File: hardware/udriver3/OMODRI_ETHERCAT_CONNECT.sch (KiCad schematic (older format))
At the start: 2 parts, among them J15 ADM6_ADF6, J16 ADM6_ADF6

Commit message: Update of the PCB routing. - F.paste updated on BGA (removed) and Q1 to Q6 (as proposed in datasheet) - F.SilkS and B.SilkS updated
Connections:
- net GND: no longer J15.C02, J15.C04, J15.C06, J15.C08, J15.D02, J15.D04, J15.D06, J15.D08, J16.A03, J16.A05, J16.A07, J16.A09, J16.B03, J16.B05, J16.B07, J16.B08, J16.B09
- new net VDD_3V3: J15.C02, J15.C04, J15.C06, J15.C08, J15.D02, J15.D04, J15.D06, J15.D08, J16.A03, J16.A05, J16.A07, J16.A09, J16.B03, J16.B05, J16.B07, J16.B08, J16.B09
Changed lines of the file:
@@
-$Comp
-L omodri_lib:ADM6_ADF6 J?
-U 1 1 5FA3E1D7
-P 3400 3250
-AR Path="/5FA3E1D7" Ref="J?"  Part="1"
-AR Path="/5F5975A7/5FA2AE4C/5FA3E1D7" Ref="J16"  Part="1"
-F 0 "J16" H 3400 3800 50  0000 L CNN
-F 1 "ADM6_ADF6" H 3400 2700 50  0000 L CNN
-F 2 "udriver3:ADF6-10-XX.X-XXX-4-X-A-XR" H 3400 3250 50  0001 C CNN
-F 3 "http://suddendocs.samtec.com/prints/adf6-xxx-xx.x-xxx-4-x-x-xr-mkt.pdf" H 3400 3250 50  0001 C CNN
-F 4 "612-ADF6-10-03.5-L-4-2-A-TR-ND" H 3400 3250 50  0001 C CNN "DigiKey"
-F 5 "3462763" H 3400 3250 50  0001 C CNN "Farnell"
-F 6 "200-ADF6-10-3.5-L42A" H 3400 3250 50  0001 C CNN "Mouser"
-F 7 "ADF6-10-03.5-L-4-2-A" H 3400 3250 50  0001 C CNN "Part No"
-F 8 "202-7885" H 3400 3250 50  0001 C CNN "RS"
-	1    3400 3250
-	1    0    0    -1
-$EndComp
 $Comp
 L omodri_lib:ADM6_ADF6 J?
@@
 Text HLabel 7350 3000 0    50   Output ~ 0
 ESC_RX1_DV
-Text HLabel 3025 2800 0    50   Output ~ 0
-ESC_RX1_ERR
 Text HLabel 4325 2900 0    50   Output ~ 0
 ESC_RX1_CLK
@@
 Text HLabel 7350 3200 0    50   Input ~ 0
 ESC_TX1_ENA
-Text HLabel 3025 3100 0    50   Output ~ 0
-ESC_TX1_CLK
 Text HLabel 7325 4700 0    50   Output ~ 0
 ESC_TX0_CLK
 Text HLabel 3025 4600 0    50   Input ~ 0
 ~ESC_PHY_RESETn~
-Text HLabel 3025 3500 0    50   Input ~ 0
-ESC_PHY_CLK_OSC
 Text HLabel 5850 3000 0    50   Input ~ 0
 ESC_PHY_CLK_INT
@@
 Text HLabel 5850 4500 0    50   Output ~ 0
 ESC_PHY0_LINKSTATUS
-Text HLabel 3025 2900 0    50   Output ~ 0
-ESC_PHY1_LINKSTATUS
 Text HLabel 3025 4800 0    50   Output ~ 0
 ECAT0_INT
-Text HLabel 3025 3300 0    50   Output ~ 0
-ECAT1_INT
 $Comp
 L omodri_lib:ADM6_ADF6 J?
@@
 Wire Wire Line
 	4400 4500 4400 4700
-$Comp
-L power:GND #PWR?
-U 1 1 5FAA5B09
-P 5925 5250
-AR Path="/5F3A3F16/5FAA5B09" Ref="#PWR?"  Part="1"
-AR Path="/5F7A5BAE/5FAA5B09" Ref="#PWR?"  Part="1"
-AR Path="/5F497A69/5FAA5B09" Ref="#PWR?"  Part="1"
-AR Path="/5F5B5760/5FAA5B09" Ref="#PWR?"  Part="1"
-AR Path="/5F5975A7/5FA2AE4C/5FAA5B09" Ref="#PWR0162"  Part="1"
-F 0 "#PWR0162" H 5925 5000 50  0001 C CNN
-F 1 "GND" H 5930 5077 50  0000 C CNN
-F 2 "" H 5925 5250 50  0001 C CNN
-F 3 "" H 5925 5250 50  0001 C CNN
-	1    5925 5250
-	1    0    0    -1
-$EndComp
-$Comp
-L power:GND #PWR?
-U 1 1 5FAAA259
-P 7425 5250
-AR Path="/5F3A3F16/5FAAA259" Ref="#PWR?"  Part="1"
-AR Path="/5F7A5BAE/5FAAA259" Ref="#PWR?"  Part="1"
-AR Path="/5F497A69/5FAAA259" Ref="#PWR?"  Part="1"
-AR Path="/5F5B5760/5FAAA259" Ref="#PWR?"  Part="1"
-AR Path="/5F5975A7/5FA2AE4C/5FAAA259" Ref="#PWR0163"  Part="1"
-F 0 "#PWR0163" H 7425 5000 50  0001 C CNN
-F 1 "GND" H 7430 5077 50  0000 C CNN
-F 2 "" H 7425 5250 50  0001 C CNN
-F 3 "" H 7425 5250 50  0001 C CNN
-	1    7425 5250
-	1    0    0    -1
-$EndComp
 Wire Wire Line
 	3200 4500 3100 4500
@@
 Wire Wire Line
 	7350 5100 7525 5100
-$Comp
-L power:GND #PWR?
-U 1 1 5F9E52B0
-P 3100 3750
-AR Path="/5F3A3F16/5F9E52B0" Ref="#PWR?"  Part="1"
-AR Path="/5F7A5BAE/5F9E52B0" Ref="#PWR?"  Part="1"
-AR Path="/5F497A69/5F9E52B0" Ref="#PWR?"  Part="1"
-AR Path="/5F5B5760/5F9E52B0" Ref="#PWR?"  Part="1"
-AR Path="/5F5975A7/5FA2AE4C/5F9E52B0" Ref="#PWR0150"  Part="1"
-F 0 "#PWR0150" H 3100 3500 50  0001 C CNN
-F 1 "GND" H 3105 3577 50  0000 C CNN
-F 2 "" H 3100 3750 50  0001 C CNN
-F 3 "" H 3100 3750 50  0001 C CNN
-	1    3100 3750
-	1    0    0    -1
-$EndComp
 Wire Wire Line
 	3100 3750 3100 3600
 Wire Wire Line
 	3100 3600 3200 3600
-$Comp
-L power:GND #PWR?
-U 1 1 5FA1341F
-P 4400 3750
-AR Path="/5F3A3F16/5FA1341F" Ref="#PWR?"  Part="1"
-AR Path="/5F7A5BAE/5FA1341F" Ref="#PWR?"  Part="1"
-AR Path="/5F497A69/5FA1341F" Ref="#PWR?"  Part="1"
-AR Path="/5F5B5760/5FA1341F" Ref="#PWR?"  Part="1"
-AR Path="/5F5975A7/5FA2AE4C/5FA1341F" Ref="#PWR0154"  Part="1"
-F 0 "#PWR0154" H 4400 3500 50  0001 C CNN
-F 1 "GND" H 4405 3577 50  0000 C CNN
-F 2 "" H 4400 3750 50  0001 C CNN
-F 3 "" H 4400 3750 50  0001 C CNN
-	1    4400 3750
-	1    0    0    -1
-$EndComp
 $Comp
 L power:GND #PWR?
@@
 Wire Wire Line
 	4400 3750 4400 3600
-Wire Wire Line
-	3025 3500 3200 3500
 Wire Wire Line
 	7350 4300 7525 4300
@@
 	6025 3500 5925 3500
 Wire Wire Line
-	3025 2800 3200 2800
-Wire Wire Line
 	4325 2800 4500 2800
 Wire Wire Line
@@
 Wire Wire Line
 	4325 2900 4500 2900
-Wire Wire Line
-	3200 2900 3025 2900
 Wire Wire Line
 	7425 3500 7425 3300
@@
 Wire Wire Line
 	3100 3600 3100 3400
-Wire Wire Line
-	3100 3000 3200 3000
 Connection ~ 3100 3600
 Wire Wire Line
@@
 Wire Wire Line
 	4500 3100 4325 3100
-Wire Wire Line
-	3200 3100 3025 3100
-Text HLabel 3025 3700 0    50   Output ~ 0
-COM_SPI_SIMO
 Text HLabel 5850 3600 0    50   Input ~ 0
 COM_SPI_SOMI
@@
 	6025 3700 5925 3700
 Wire Wire Line
-	3200 3700 3025 3700
-Wire Wire Line
 	4500 3700 4325 3700
 Wire Wire Line
 	3100 3200 3200 3200
-Connection ~ 3100 3200
-Wire Wire Line
-	3100 3200 3100 3000
 Wire Wire Line
 	4500 3200 4400 3200
@@
 	6025 3200 5850 3200
 Wire Wire Line
-	3200 3300 3025 3300
-Wire Wire Line
 	7525 3300 7425 3300
 Connection ~ 7425 3300
@@
 Wire Wire Line
 	5925 3700 5925 3750
+$Comp
+L omodri_lib:ADM6_ADF6 J?
+U 1 1 5FA3E1D7
+P 3400 3250
+AR Path="/5FA3E1D7" Ref="J?"  Part="1"
+AR Path="/5F5975A7/5FA2AE4C/5FA3E1D7" Ref="J16"  Part="1"
+F 0 "J16" H 3400 3800 50  0000 L CNN
+F 1 "ADM6_ADF6" H 3400 2700 50  0000 L CNN
+F 2 "udriver3:ADF6-10-XX.X-XXX-4-X-A-XR" H 3400 3250 50  0001 C CNN
+F 3 "http://suddendocs.samtec.com/prints/adf6-xxx-xx.x-xxx-4-x-x-xr-mkt.pdf" H 3400 3250 50  0001 C CNN
+F 4 "612-ADF6-10-03.5-L-4-2-A-TR-ND" H 3400 3250 50  0001 C CNN "DigiKey"
+F 5 "3462763" H 3400 3250 50  0001 C CNN "Farnell"
+F 6 "200-ADF6-10-3.5-L42A" H 3400 3250 50  0001 C CNN "Mouser"
+F 7 "ADF6-10-03.5-L-4-2-A" H 3400 3250 50  0001 C CNN "Part No"
+F 8 "202-7885" H 3400 3250 50  0001 C CNN "RS"
+	1    3400 3250
+	1    0    0    -1
+$EndComp
+Connection ~ 3100 3200
+Wire Wire Line
+	3100 3200 3100 3000
+Wire Wire Line
+	3100 3000 3200 3000
+Text GLabel 3100 3750 3    50   Input ~ 0
+VDD_3V3
+Wire Wire Line
+	3200 3300 3025 3300
+Wire Wire Line
+	3200 3700 3025 3700
+Text HLabel 3025 3700 0    50   Output ~ 0
+COM_SPI_SIMO
+Wire Wire Line
+	3200 3100 3025 3100
+Wire Wire Line
+	3200 2900 3025 2900
+Wire Wire Line
+	3025 2800 3200 2800
+Wire Wire Line
+	3025 3500 3200 3500
+Text HLabel 3025 3300 0    50   Output ~ 0
+ECAT1_INT
+Text HLabel 3025 2900 0    50   Output ~ 0
+ESC_PHY1_LINKSTATUS
+Text HLabel 3025 3500 0    50   Input ~ 0
+ESC_PHY_CLK_OSC
+Text HLabel 3025 3100 0    50   Output ~ 0
+ESC_TX1_CLK
+Text HLabel 3025 2800 0    50   Output ~ 0
+ESC_RX1_ERR
+Text GLabel 4400 3750 3    50   Input ~ 0
+VDD_3V3
+Text GLabel 5925 5250 3    50   Input ~ 0
+VDD_3V3
+Text GLabel 7425 5250 3    50   Input ~ 0
+VDD_3V3
 $EndSCHEMATC

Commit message: Revision of the OMODRI PCB including: - 5V power distribution on extension connector - New GPIO pin available on extension connector for SPI chip select (SSI sensors) - Connectors labels - logos - BGA solder mask/past updated
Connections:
- net GND: no longer J16.C10, J16.D10
- net VDD_3V3: no longer J16.B08
- new net 5V0: J16.C10, J16.D10
- new net ~SPI_CS2n~: J16.B08
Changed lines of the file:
@@
-$Comp
-L omodri_lib:ADM6_ADF6 J?
-U 2 1 5FA3E1DD
-P 4700 3250
-AR Path="/5FA3E1DD" Ref="J?"  Part="2"
-AR Path="/5F5975A7/5FA2AE4C/5FA3E1DD" Ref="J16"  Part="2"
-F 0 "J16" H 4700 3800 50  0000 L CNN
-F 1 "ADM6_ADF6" H 4700 2700 50  0000 L CNN
-F 2 "udriver3:ADF6-10-XX.X-XXX-4-X-A-XR" H 4700 3250 50  0001 C CNN
-F 3 "http://suddendocs.samtec.com/prints/adf6-xxx-xx.x-xxx-4-x-x-xr-mkt.pdf" H 4700 3250 50  0001 C CNN
-F 4 "612-ADF6-10-03.5-L-4-2-A-TR-ND" H 4700 3250 50  0001 C CNN "DigiKey"
-F 5 "3462763" H 4700 3250 50  0001 C CNN "Farnell"
-F 6 "200-ADF6-10-3.5-L42A" H 4700 3250 50  0001 C CNN "Mouser"
-F 7 "ADF6-10-03.5-L-4-2-A" H 4700 3250 50  0001 C CNN "Part No"
-F 8 "202-7885" H 4700 3250 50  0001 C CNN "RS"
-	2    4700 3250
-	1    0    0    -1
-$EndComp
 $Comp
 L omodri_lib:ADM6_ADF6 J?
@@
 Connection ~ 3100 3600
 Wire Wire Line
-	4400 3600 4400 3500
-Wire Wire Line
 	4400 3000 4500 3000
 Connection ~ 4400 3600
@@
 COM_SPI_CLK
 Wire Wire Line
-	7425 3500 7425 3700
-Wire Wire Line
-	6025 3700 5925 3700
-Wire Wire Line
 	4500 3700 4325 3700
 Wire Wire Line
@@
 	6025 3400 5850 3400
 Wire Wire Line
-	4500 3500 4400 3500
-Connection ~ 4400 3500
-Wire Wire Line
-	4400 3500 4400 3400
-Wire Wire Line
-	5925 3500 5925 3700
-Wire Wire Line
 	6025 3600 5850 3600
-Connection ~ 7425 3700
-Wire Wire Line
-	7425 3700 7425 3750
-Wire Wire Line
-	7425 3700 7525 3700
-Connection ~ 5925 3700
-Wire Wire Line
-	5925 3700 5925 3750
 $Comp
 L omodri_lib:ADM6_ADF6 J?
@@
 Text GLabel 7425 5250 3    50   Input ~ 0
 VDD_3V3
+Text HLabel 4325 3500 0    50   Output ~ 0
+~SPI_CS2n~
+Wire Wire Line
+	4400 3400 4400 3600
+$Comp
+L omodri_lib:ADM6_ADF6 J?
+U 2 1 5FA3E1DD
+P 4700 3250
+AR Path="/5FA3E1DD" Ref="J?"  Part="2"
+AR Path="/5F5975A7/5FA2AE4C/5FA3E1DD" Ref="J16"  Part="2"
+F 0 "J16" H 4700 3800 50  0000 L CNN
+F 1 "ADM6_ADF6" H 4700 2700 50  0000 L CNN
+F 2 "udriver3:ADF6-10-XX.X-XXX-4-X-A-XR" H 4700 3250 50  0001 C CNN
+F 3 "http://suddendocs.samtec.com/prints/adf6-xxx-xx.x-xxx-4-x-x-xr-mkt.pdf" H 4700 3250 50  0001 C CNN
+F 4 "612-ADF6-10-03.5-L-4-2-A-TR-ND" H 4700 3250 50  0001 C CNN "DigiKey"
+F 5 "3462763" H 4700 3250 50  0001 C CNN "Farnell"
+F 6 "200-ADF6-10-3.5-L42A" H 4700 3250 50  0001 C CNN "Mouser"
+F 7 "ADF6-10-03.5-L-4-2-A" H 4700 3250 50  0001 C CNN "Part No"
+F 8 "202-7885" H 4700 3250 50  0001 C CNN "RS"
+	2    4700 3250
+	1    0    0    -1
+$EndComp
+Wire Wire Line
+	4500 3500 4325 3500
+Wire Wire Line
+	7425 3500 7425 3750
+Text GLabel 7350 3700 0    50   Input ~ 0
+5V0
+Text GLabel 5850 3700 0    50   Input ~ 0
+5V0
+Wire Wire Line
+	5925 3500 5925 3750
+Wire Wire Line
+	5850 3700 6025 3700
+Wire Wire Line
+	7350 3700 7525 3700
 $EndSCHEMATC

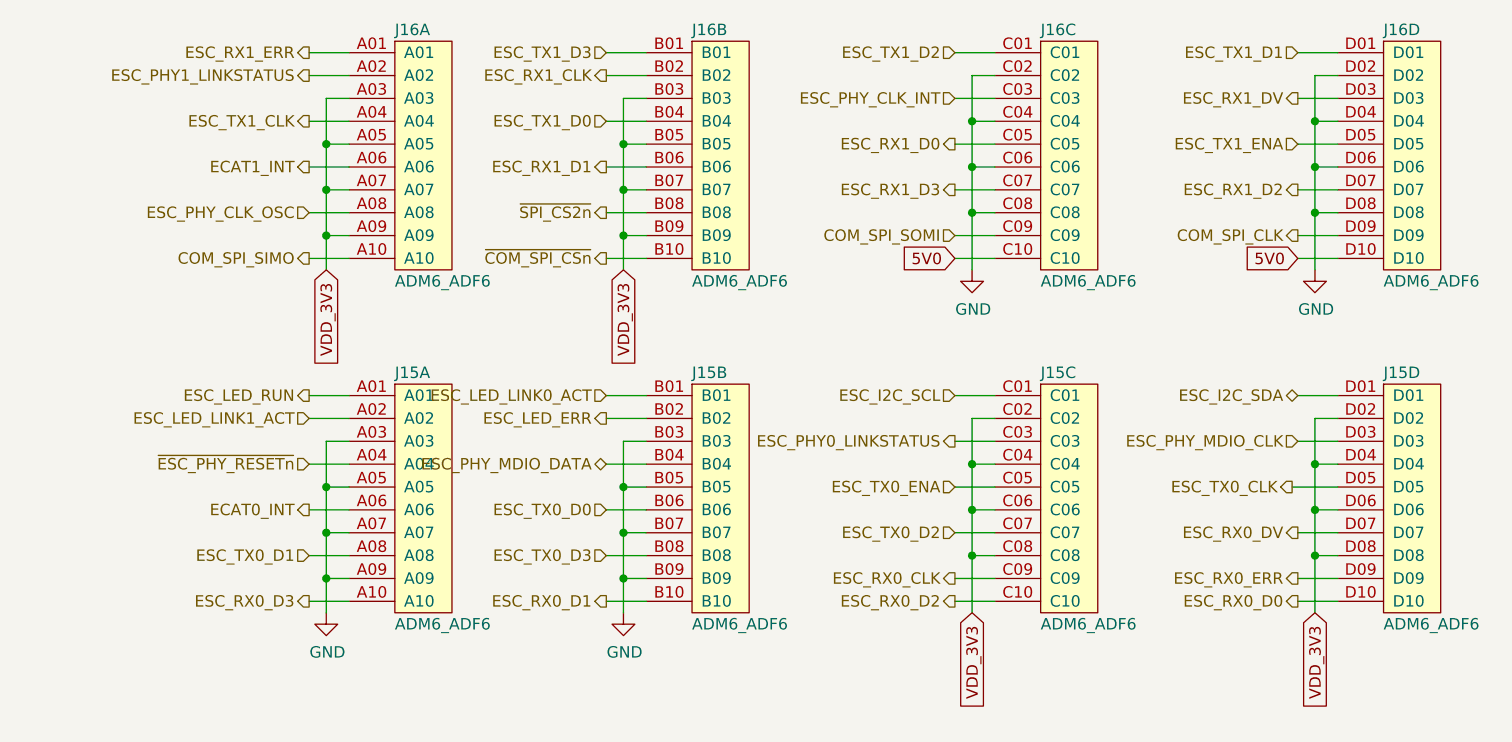
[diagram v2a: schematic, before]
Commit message: Update of µOmodri: - 25MHz oscillator signal removed (ECAT_PHY_CLK is still present) - 1x Analog signal available on extension connector - SPI on extension connector replaced. Previously SPI3/COM SPI, also available on J2, replaced by general purpose SPI2 also available on J1 connector.
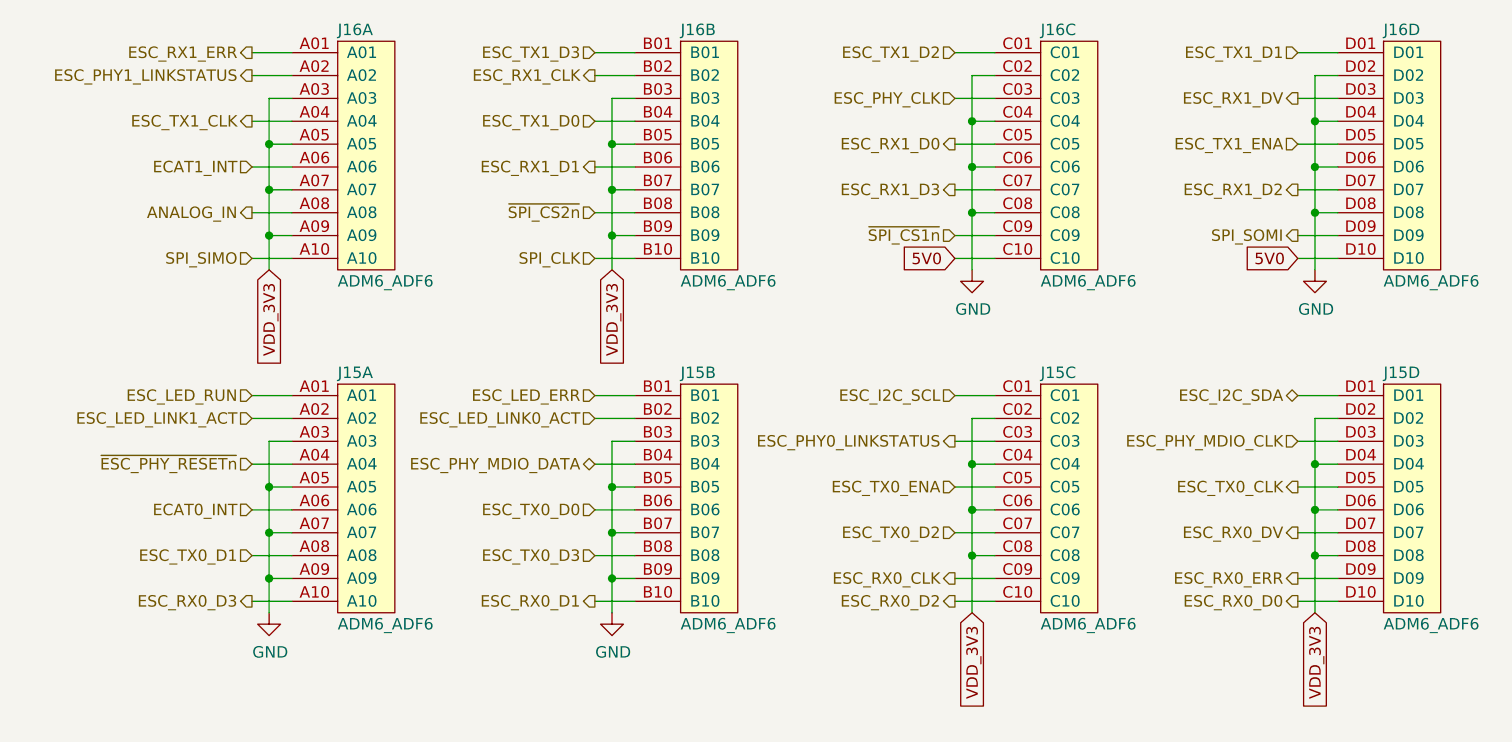
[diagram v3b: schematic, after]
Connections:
- net ESC_LED_ERR: now also J15.B01; no longer J15.B02
- net ESC_LED_LINK0_ACT: now also J15.B02; no longer J15.B01
- net COM_SPI_CLK renamed SPI_SOMI
- net COM_SPI_SIMO renamed SPI_SIMO
- net COM_SPI_SOMI renamed ~SPI_CS1n~
- net ESC_PHY_CLK_INT renamed ESC_PHY_CLK
- net ESC_PHY_CLK_OSC renamed ANALOG_IN
- net ~COM_SPI_CSn~ renamed SPI_CLK
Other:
- moved on the sheet: J15A, J15B, J16A, J16B

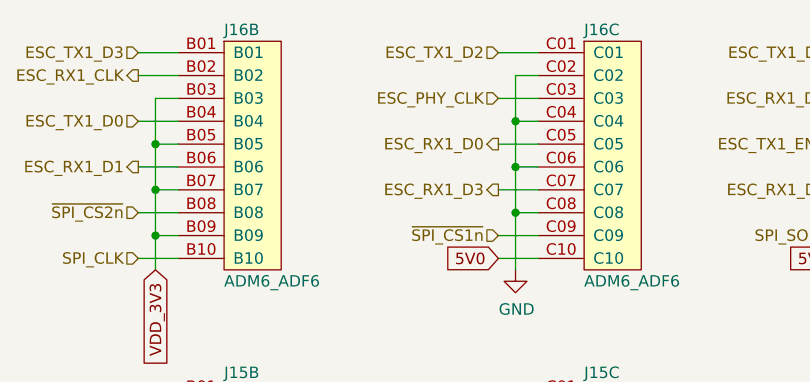
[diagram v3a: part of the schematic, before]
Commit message: Update of the 25MHz clock signal available on extension connector J16 from ESC_PHY_CLK to 25MHz TCXO oscillator. Update of the gerber files. Update of the title blocks of the schematics.
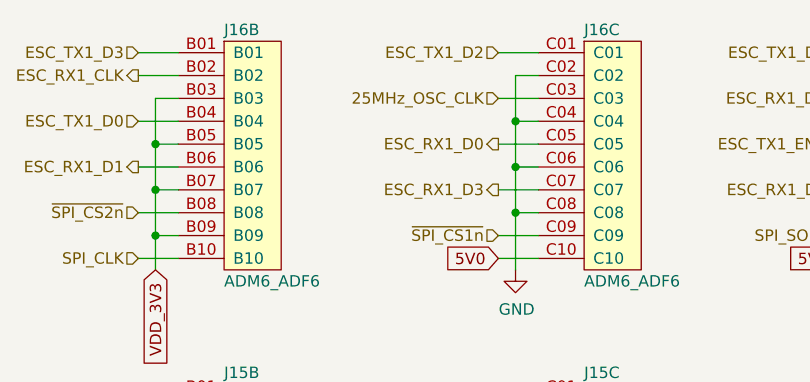
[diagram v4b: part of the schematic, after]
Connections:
- net ESC_PHY_CLK renamed 25MHz_OSC_CLK
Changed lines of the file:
@@
 encoding utf-8
 Sheet 14 19
-Title ""
-Date ""
-Rev ""
-Comp ""
+Title "Open MOtor DRiver Initiative (OMODRI)"
+Date "2020-12-16"
+Rev "1.0"
+Comp "LAAS/CNRS"
 Comment1 ""
 Comment2 ""
@@
 ~ESC_PHY_RESETn~
 Text HLabel 5850 3000 0    50   Input ~ 0
-ESC_PHY_CLK
+25MHz_OSC_CLK
 Text HLabel 7350 4300 0    50   BiDi ~ 0
 ESC_I2C_SDA

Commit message: update ADF6 connector footprint, add revision number, clean FAB layers, update fab files
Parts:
- J15, J16: footprint udriver3:ADF6-10-XX.X-XXX-4-X-A-XR -> footprint:SAMTEC_ADF6-10-03.5-L-4-2-A-TR
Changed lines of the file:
@@
 $Descr A4 11693 8268
 encoding utf-8
-Sheet 14 19
+Sheet 19 19
 Title "Open MOtor DRiver Initiative (OMODRI)"
 Date "2020-12-16"
-Rev "1.0"
+Rev "1.1"
 Comp "LAAS/CNRS"
 Comment1 ""
@@
 F 0 "J16" H 6225 3800 50  0000 L CNN
 F 1 "ADM6_ADF6" H 6225 2700 50  0000 L CNN
-F 2 "udriver3:ADF6-10-XX.X-XXX-4-X-A-XR" H 6225 3250 50  0001 C CNN
+F 2 "footprint:SAMTEC_ADF6-10-03.5-L-4-2-A-TR" H 6225 3250 50  0001 C CNN
 F 3 "http://suddendocs.samtec.com/prints/adf6-xxx-xx.x-xxx-4-x-x-xr-mkt.pdf" H 6225 3250 50  0001 C CNN
 F 4 "612-ADF6-10-03.5-L-4-2-A-TR-ND" H 6225 3250 50  0001 C CNN "DigiKey"
@@
 F 0 "J16" H 7725 3800 50  0000 L CNN
 F 1 "ADM6_ADF6" H 7725 2700 50  0000 L CNN
-F 2 "udriver3:ADF6-10-XX.X-XXX-4-X-A-XR" H 7725 3250 50  0001 C CNN
+F 2 "footprint:SAMTEC_ADF6-10-03.5-L-4-2-A-TR" H 7725 3250 50  0001 C CNN
 F 3 "http://suddendocs.samtec.com/prints/adf6-xxx-xx.x-xxx-4-x-x-xr-mkt.pdf" H 7725 3250 50  0001 C CNN
 F 4 "612-ADF6-10-03.5-L-4-2-A-TR-ND" H 7725 3250 50  0001 C CNN "DigiKey"
@@
 F 0 "J15" H 3150 5300 50  0000 L CNN
 F 1 "ADM6_ADF6" H 3150 4200 50  0000 L CNN
-F 2 "udriver3:ADF6-10-XX.X-XXX-4-X-A-XR" H 3150 4750 50  0001 C CNN
+F 2 "footprint:SAMTEC_ADF6-10-03.5-L-4-2-A-TR" H 3150 4750 50  0001 C CNN
 F 3 "http://suddendocs.samtec.com/prints/adf6-xxx-xx.x-xxx-4-x-x-xr-mkt.pdf" H 3150 4750 50  0001 C CNN
 F 4 "612-ADF6-10-03.5-L-4-2-A-TR-ND" H 3150 4750 50  0001 C CNN "DigiKey"
@@
 F 0 "J15" H 7725 5300 50  0000 L CNN
 F 1 "ADM6_ADF6" H 7725 4200 50  0000 L CNN
-F 2 "udriver3:ADF6-10-XX.X-XXX-4-X-A-XR" H 7725 4750 50  0001 C CNN
+F 2 "footprint:SAMTEC_ADF6-10-03.5-L-4-2-A-TR" H 7725 4750 50  0001 C CNN
 F 3 "http://suddendocs.samtec.com/prints/adf6-xxx-xx.x-xxx-4-x-x-xr-mkt.pdf" H 7725 4750 50  0001 C CNN
 F 4 "612-ADF6-10-03.5-L-4-2-A-TR-ND" H 7725 4750 50  0001 C CNN "DigiKey"
@@
 F 0 "J15" H 6225 5300 50  0000 L CNN
 F 1 "ADM6_ADF6" H 6225 4200 50  0000 L CNN
-F 2 "udriver3:ADF6-10-XX.X-XXX-4-X-A-XR" H 6225 4750 50  0001 C CNN
+F 2 "footprint:SAMTEC_ADF6-10-03.5-L-4-2-A-TR" H 6225 4750 50  0001 C CNN
 F 3 "http://suddendocs.samtec.com/prints/adf6-xxx-xx.x-xxx-4-x-x-xr-mkt.pdf" H 6225 4750 50  0001 C CNN
 F 4 "612-ADF6-10-03.5-L-4-2-A-TR-ND" H 6225 4750 50  0001 C CNN "DigiKey"
@@
 F 0 "J15" H 4650 5300 50  0000 L CNN
 F 1 "ADM6_ADF6" H 4650 4200 50  0000 L CNN
-F 2 "udriver3:ADF6-10-XX.X-XXX-4-X-A-XR" H 4650 4750 50  0001 C CNN
+F 2 "footprint:SAMTEC_ADF6-10-03.5-L-4-2-A-TR" H 4650 4750 50  0001 C CNN
 F 3 "http://suddendocs.samtec.com/prints/adf6-xxx-xx.x-xxx-4-x-x-xr-mkt.pdf" H 4650 4750 50  0001 C CNN
 F 4 "612-ADF6-10-03.5-L-4-2-A-TR-ND" H 4650 4750 50  0001 C CNN "DigiKey"
@@
 F 0 "J16" H 3150 3800 50  0000 L CNN
 F 1 "ADM6_ADF6" H 3150 2700 50  0000 L CNN
-F 2 "udriver3:ADF6-10-XX.X-XXX-4-X-A-XR" H 3150 3250 50  0001 C CNN
+F 2 "footprint:SAMTEC_ADF6-10-03.5-L-4-2-A-TR" H 3150 3250 50  0001 C CNN
 F 3 "http://suddendocs.samtec.com/prints/adf6-xxx-xx.x-xxx-4-x-x-xr-mkt.pdf" H 3150 3250 50  0001 C CNN
 F 4 "612-ADF6-10-03.5-L-4-2-A-TR-ND" H 3150 3250 50  0001 C CNN "DigiKey"
@@
 F 0 "J16" H 4650 3800 50  0000 L CNN
 F 1 "ADM6_ADF6" H 4650 2700 50  0000 L CNN
-F 2 "udriver3:ADF6-10-XX.X-XXX-4-X-A-XR" H 4650 3250 50  0001 C CNN
+F 2 "footprint:SAMTEC_ADF6-10-03.5-L-4-2-A-TR" H 4650 3250 50  0001 C CNN
 F 3 "http://suddendocs.samtec.com/prints/adf6-xxx-xx.x-xxx-4-x-x-xr-mkt.pdf" H 4650 3250 50  0001 C CNN
 F 4 "612-ADF6-10-03.5-L-4-2-A-TR-ND" H 4650 3250 50  0001 C CNN "DigiKey"
